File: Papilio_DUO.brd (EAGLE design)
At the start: 100 x 56 mm, 116 parts, among them IC1 FT2232H, SW1 SWITCH-2CH-6P-3010010P1, SW2 EVQQ2, U1 ARDUINO_MEGA_SHIELD, U101 ATMEGA32U4-XUMU, U2 LTC3419EMS, U3 93C46B, X1 12MHz, Y1 16MHz KX-7

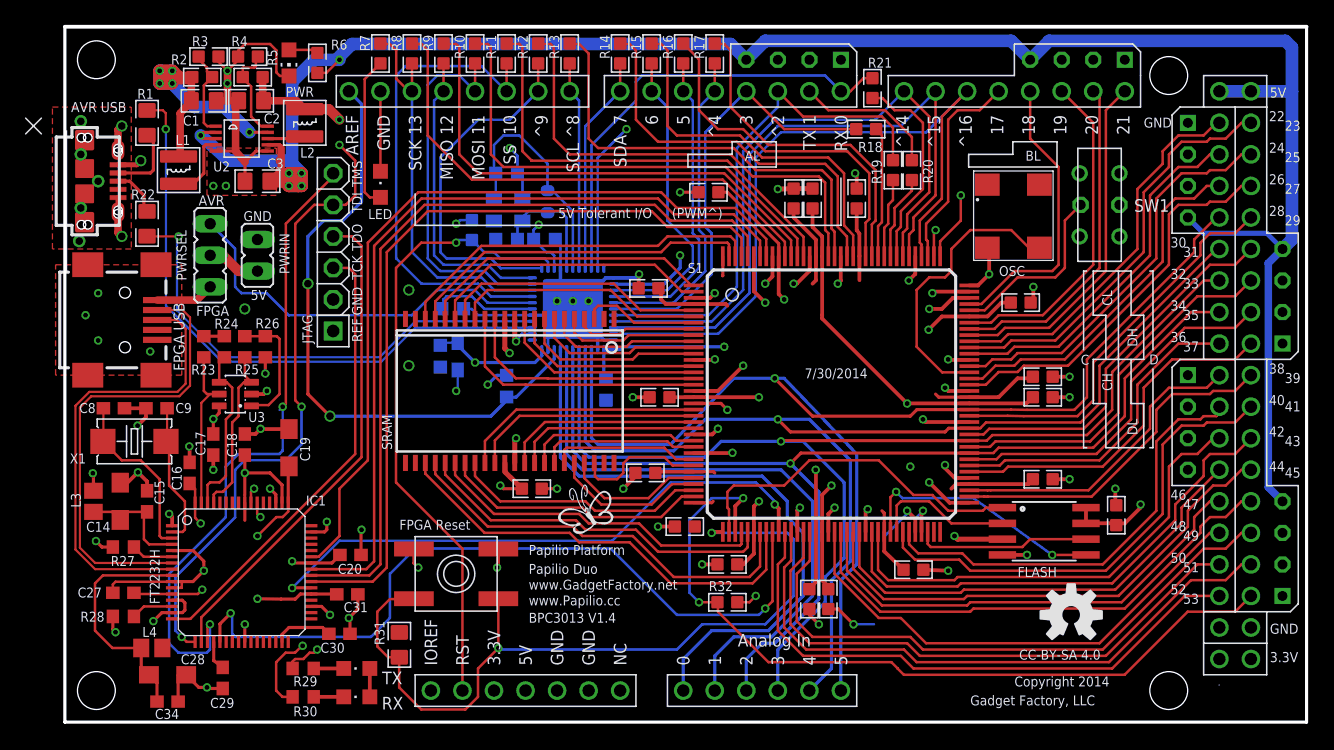
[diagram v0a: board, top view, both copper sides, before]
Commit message: Added TQFP footprint
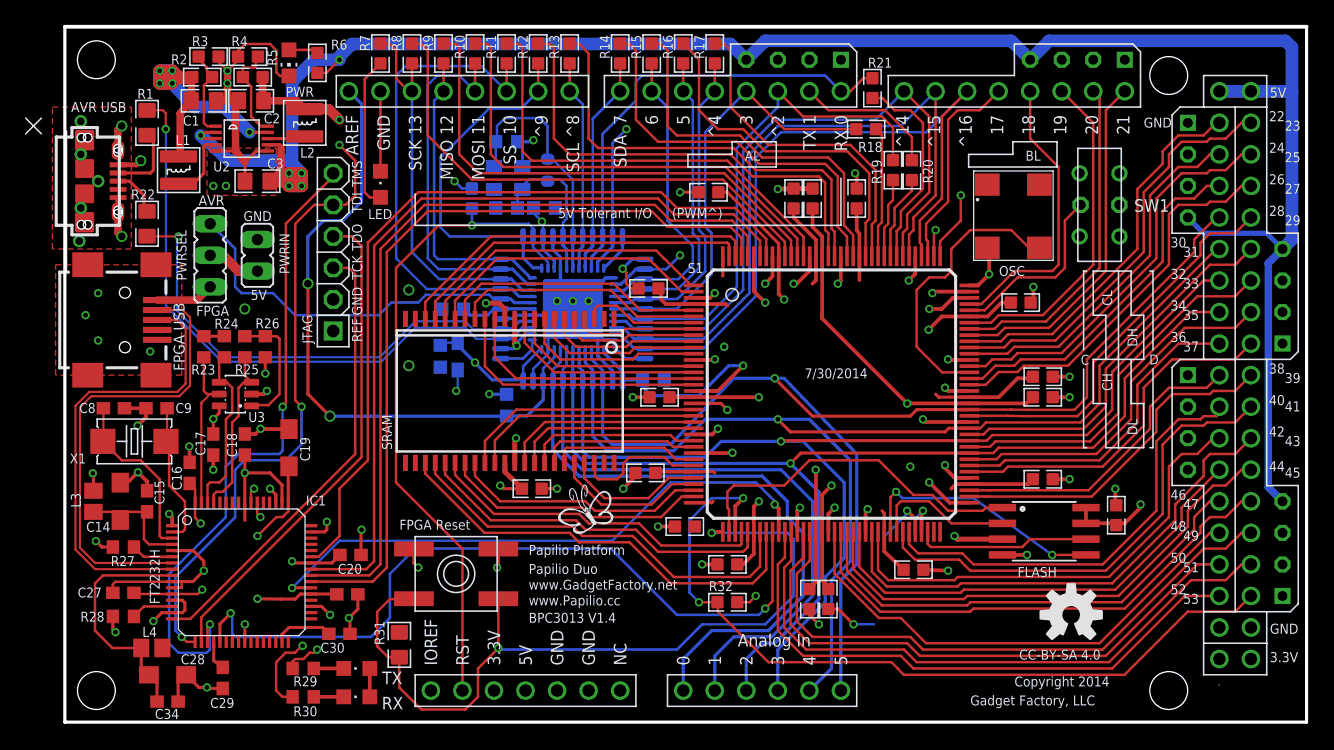
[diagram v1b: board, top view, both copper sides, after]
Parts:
- added U102: ATMEGA32U4-XUAU, SmartPrj:TQFP44-PAD
- moved C101 3.89 mm to (47.4, 27.5), turned to 180 degrees
- moved R109 2.54 mm to (38.9, 44.5)
- moved C105 2.54 mm to (38.6, 41.4)
- moved C106 2.54 mm to (35.6, 41.4)
- moved C107 2.54 mm to (35.6, 46.7)
- moved R110 2.54 mm to (32.8, 42.2)
- moved Y1 2.54 mm to (35.7, 43.8)
- moved C102 1.52 mm to (35.6, 25.5)
- turned C103 to 0 degrees
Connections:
- new net N$1: U101.22, U102.22
- net 3V3: now also U102.14, U102.2, U102.34
- net 5V_ARDUINO: now also U102.7
- net ARD_RESET: now also U102.13
- net AREF: now also U102.42
- net ATMEGA_A0: now also U102.41
- net ATMEGA_A1: now also U102.40
- net ATMEGA_D0/RX: now also U102.20
- net ATMEGA_D1/TX: now also U102.21
- net ATMEGA_D2: now also U102.29
- net ATMEGA_D3: now also U102.28
- net ATMEGA_D4: now also U102.27
- net ATMEGA_D5*: now also U102.26
- net ATMEGA_D6*: now also U102.25
- net ATMEGA_D7: now also U102.19
- net ATMEGA_IO10*: now also U102.8
- net ATMEGA_IO11*: now also U102.10
- net ATMEGA_IO12: now also U102.11
- net ATMEGA_IO13*: now also U102.9
- net ATMEGA_IO8: now also U102.18
- net ATMEGA_IO9*: now also U102.12
- net AVCC: now also U102.24, U102.44
- net AVRUSB_N: now also U102.3
- net AVRUSB_P: now also U102.4
- net GND: now also U102.15, U102.23, U102.33, U102.35, U102.43, U102.5, U102.P$1
- net MEGA_D14: now also U102.30
- net MEGA_D15: now also U102.31
- net MEGA_D16: now also U102.32
- net MEGA_D28/A5: now also U102.36
- net MEGA_D30/A4: now also U102.37
- net MEGA_D32/A3: now also U102.38
- net MEGA_D34/A2: now also U102.39
- net NC: now also U102.1
- net UCAP: now also U102.6
- net XTAL1: now also U102.17
- net XTAL2: now also U102.16
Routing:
- net GND: track 205.9 -> 214.9 mm
- net 3V3: track 208.7 -> 217.3 mm
- net ARD_RESET: track 82.9 -> 87.4 mm
- net NC: track 0.00 -> 3.68 mm
- net N$1: track 0.00 -> 3.15 mm
- net XTAL2: track 10.3 -> 13.0 mm
- net UCAP: track 8.47 -> 5.93 mm
- net XTAL1: track 19.6 -> 21.2 mm
- net AREF: track 50.9 -> 52.1 mm
- net AVCC: track 37.8 -> 38.9 mm
- net MEGA_D16: track 58.0 -> 59.0 mm
- net AVRUSB_N: track 49.6 -> 50.4 mm
- net MEGA_D15: track 54.5 -> 55.3 mm
- net MEGA_D28/A5: track 99.3 -> 98.6 mm
- net MEGA_D30/A4: track 95.2 -> 94.7 mm
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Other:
- board text added: "KICKSTARTER EDITION"

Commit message: Version 1.5 - Kickstarter Edition
-Added TQFP footprint for the ATmega32U4
-Changed values for LED resistors so they won't be so bright. R7, R29,
R30
-Changed size of the EEPROM used by the FT2232H chip from 1K to 2K. This
allows us to look like official Xilinx Cable. U3
-Fixed up some silkscreen markings to make it more obvious how to place
the parts.
-Added the Kickstarter Special Edition Marking
-Changed PCB color to Black
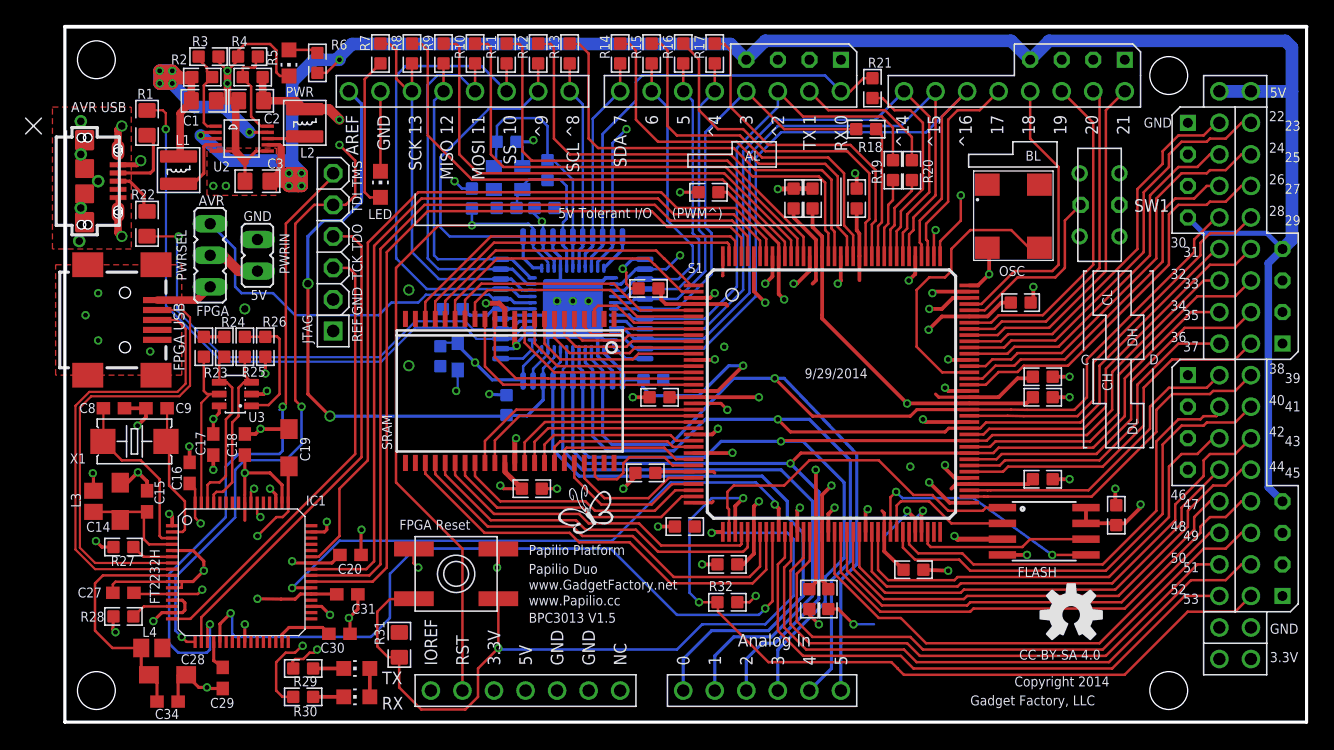
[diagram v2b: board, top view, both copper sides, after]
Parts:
- C101, C102, C103, C104, C105, C106, C107: device SmartPrj:C0603K -> GadgetFactory:0603
- LED: device led:CHIPLED_0805 -> led:CHIP-LED0805
- R109: device SmartPrj:R0603-ROUND -> GadgetFactory:0603
- R23, R24, R25, R26, R27, R28: device dp_devices:R603 -> GadgetFactory:0603
- R29, R30: value 470 -> 1K; device dp_devices:R603 -> GadgetFactory:0603
- R7: value 1K -> 4.7K
- RX, TX: device dp_devices:LED-805 -> led:CHIP-LED0805
- U3: value 93C46B -> 93C56B
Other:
- board text added: "9/29/2014"
- board text added: "BPC3013 V1.5"
- board text removed: "7/30/2014"
- board text removed: "BPC3013 V1.4"

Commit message: Version 1.6
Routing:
- net GND: track 215.1 -> 208.8 mm
- net 3V3: track 217.4 -> 214.0 mm
- net ARD_RESET: track 87.4 -> 85.3 mm
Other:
- board text added: "1/7/2015"
- board text added: "BPC3013 V1.6"
- board text removed: "9/29/2014"
- board text removed: "BPC3013 V1.5"
- board text removed: "KICKSTARTER EDITION"
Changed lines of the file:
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@@
 <layer number="127" name="_tValues" color="7" fill="1" visible="no" active="no"/>
 <layer number="128" name="_bValues" color="7" fill="1" visible="no" active="no"/>
-<layer number="130" name="tSilk" color="16" fill="1" visible="no" active="yes"/>
+<layer number="130" name="tSilk" color="16" fill="1" visible="yes" active="yes"/>
 <layer number="131" name="prix" color="7" fill="1" visible="no" active="yes"/>
 <layer number="132" name="test" color="7" fill="1" visible="no" active="yes"/>
@@
 <text x="37.354" y="13.462" size="0.8" layer="130" font="vector" ratio="14">Papilio Platform</text>
 <text x="37.354" y="11.938" size="0.8" layer="130" font="vector" ratio="14">Papilio Duo</text>
-<text x="37.354" y="8.001" size="0.8" layer="130" font="vector" ratio="14">BPC3013 V1.5</text>
+<text x="37.354" y="8.001" size="0.8" layer="130" font="vector" ratio="14">BPC3013 V1.6</text>
 <text x="37.354" y="10.668" size="0.8" layer="130" font="vector" ratio="14">www.GadgetFactory.net</text>
 <text x="76.47" y="2.8702" size="0.8" layer="130" font="vector" ratio="14">Copyright 2014</text>
 <text x="72.914" y="1.3462" size="0.8" layer="130" font="vector" ratio="14">Gadget Factory, LLC</text>
-<text x="59.579" y="27.686" size="0.8" layer="130" font="vector" ratio="14">9/29/2014</text>
+<text x="59.579" y="27.686" size="0.8" layer="130" font="vector" ratio="14">1/7/2015</text>
 <text x="26.94" y="15.494" size="0.8" layer="130" font="vector" ratio="14">FPGA Reset</text>
 <text x="84.344" y="33.528" size="0.8" layer="130" font="vector" ratio="14" rot="R90">CL</text>
@@
 <wire x1="87.63" y1="22.098" x2="87.376" y2="22.098" width="0.127" layer="130"/>
 <text x="81.28" y="5.08" size="1.778" layer="200" font="vector" ratio="15" rot="MR0">To get started visit: Duo.GadgetFactory.net</text>
-<text x="49.53" y="20.32" size="2.54" layer="200" font="vector" ratio="15" rot="MR0">KICKSTARTER EDITION</text>
 </plain>
 <attributes>
@@
 <param name="dpGapFactor" value="2.5"/>
 <param name="checkGrid" value="0"/>
-<param name="checkAngle" value="0"/>
+<param name="checkAngle" value="1"/>
 <param name="checkFont" value="1"/>
 <param name="checkRestrict" value="0"/>
@@
 <wire x1="36.23" y1="22.752" x2="36.338" y2="22.86" width="0.4064" layer="1"/>
 <via x="36.338" y="22.86" extent="1-16" drill="0.381"/>
-<wire x1="48.276" y1="37.465" x2="45.228" y2="36.068" width="0.2032" layer="2"/>
 <contactref element="C102" pad="1"/>
 <contactref element="C103" pad="2"/>
@@
 <via x="39.64" y="33.909" extent="1-16" drill="0.381"/>
 <via x="34.179" y="26.416" extent="1-16" drill="0.381"/>
-<wire x1="34.179" y1="26.416" x2="34.052" y2="27.686" width="0.254" layer="2"/>
 <via x="37.735" y="46.863" extent="1-16" drill="0.381"/>
 <wire x1="77.778" y1="33.782" x2="77.994" y2="33.782" width="0.2032" layer="1"/>
@@
 <wire x1="67.7832" y1="16.7386" x2="67.7832" y2="16.9672" width="0.2032" layer="16"/>
 <wire x1="67.7832" y1="16.9672" x2="67.834" y2="17.018" width="0.2032" layer="16"/>
-<wire x1="65.1608" y1="7.8802" x2="63.516" y2="7.874" width="0.2032" layer="16"/>
 <wire x1="72.838" y1="17.666" x2="71.25" y2="17.666" width="0.3048" layer="1"/>
 <wire x1="71.25" y1="17.666" x2="69.612" y2="19.304" width="0.3048" layer="1"/>
@@
 <via x="38.4208" y="40.3098" extent="1-16" drill="0.381"/>
 <via x="31.385" y="43.561" extent="1-16" drill="0.381"/>
-<wire x1="31.385" y1="43.561" x2="31.004" y2="40.132" width="0.2032" layer="3"/>
 <via x="27.702" y="28.702" extent="1-16" drill="0.6096"/>
 <via x="27.702" y="34.798" extent="1-16" drill="0.6096"/>
@@
 <wire x1="55.488" y1="37.516" x2="55.488" y2="34.698" width="0.3048" layer="1"/>
 <wire x1="54.88" y1="37.084" x2="53.102" y2="38.862" width="0.2032" layer="3"/>
-<wire x1="53.102" y1="38.862" x2="31.766" y2="38.862" width="0.2032" layer="3"/>
-<wire x1="31.766" y1="38.862" x2="32.782" y2="40.005" width="0.2032" layer="3"/>
+<wire x1="53.102" y1="38.862" x2="33.925" y2="38.862" width="0.2032" layer="3"/>
 <contactref element="U1" pad="RES"/>
 <wire x1="32.02" y1="2.54" x2="32.02" y2="13.954" width="0.2032" layer="1"/>
@@
 <wire x1="38.91" y1="37.036" x2="37.71" y2="38.236" width="0.2032" layer="16"/>
 <wire x1="37.71" y1="39.074" x2="37.71" y2="38.236" width="0.2032" layer="16"/>
+<wire x1="33.925" y1="38.862" x2="32.782" y2="40.005" width="0.2032" layer="3"/>
 </signal>
 <signal name="SW1">
